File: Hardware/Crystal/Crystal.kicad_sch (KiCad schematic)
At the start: 46 parts, among them J1 USB_B_Micro, U1 AP63205WU, U2 NCP1117-3.3_SOT223, U3 ESP32-C3-WROOM-02, U4 TXS0102DCT, U5 TXS0108EPW

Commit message: Revised L1 for possible 2A output, cleaner fill zones
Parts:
- L1: footprint Inductor_SMD:L_1008_2520Metric_Pad1.43x2.20mm_HandSolder -> Inductor_SMD_Wurth:L_Wurth_WE-LQSH-4020; MFG Murata Electronics -> Wuerth Electronik; PN LQM2HPN4R7MGCL -> 74405042047
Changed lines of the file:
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@@
       (effects (font (size 1.27 1.27)))
     )
-    (property "Footprint" "Inductor_SMD:L_1008_2520Metric_Pad1.43x2.20mm_HandSolder" (at 208.28 30.48 0)
+    (property "Footprint" "Inductor_SMD_Wurth:L_Wurth_WE-LQSH-4020" (at 208.28 30.48 0)
       (effects (font (size 1.27 1.27)) hide)
     )
-    (property "Datasheet" "https://www.mouser.com/datasheet/2/281/1/JELF243B_0025-1634213.pdf" (at 208.28 30.48 0)
+    (property "Datasheet" "https://www.we-online.com/catalog/datasheet/74405042047.pdf" (at 208.28 30.48 0)
       (effects (font (size 1.27 1.27)) hide)
     )
-    (property "MFG" "Murata Electronics" (at 208.28 30.48 0)
+    (property "MFG" "Wuerth Electronik" (at 208.28 30.48 0)
       (effects (font (size 1.27 1.27)) hide)
     )
-    (property "PN" "LQM2HPN4R7MGCL " (at 208.28 30.48 0)
+    (property "PN" "74405042047" (at 208.28 30.48 0)
       (effects (font (size 1.27 1.27)) hide)
     )

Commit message: Added note about VIN plug, BOM cleanup.
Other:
- note added: "Wuerth WR-TBL Plug: Mouser 691361300002 Socket: 691322310002"
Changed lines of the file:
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@@
+    (effects (font (size 1.27 1.27)) (justify left bottom))
+  )
+  (text "Wuerth WR-TBL\nPlug: Mouser 691361300002 \nSocket: 691322310002 "
+    (at 134.62 41.275 0)
     (effects (font (size 1.27 1.27)) (justify left bottom))
   )

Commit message: Checkpoint
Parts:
- added D9: Blue, LED_SMD:LED_1206_3216Metric, symbol Device:LED_Small
- added R17: 1k, Resistor_SMD:R_1206_3216Metric, symbol Device:R
- CB1: now not fitted; now left out of the parts list
- D1: value LED -> Red
- L1: footprint Inductor_SMD_Wurth:L_Wurth_WE-LQSH-4020 -> Inductor_SMD:L_1008_2520Metric_Pad1.43x2.20mm_HandSolder; MFG Wuerth Electronik -> Murata Electronics; PN 74405042047 -> LQM2HPN4R7MGCL
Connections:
- net GND: now also R17.2
- net at TTY1.2 (Pin_2), U4.8 (B1): now also D9.2 (A)
- removed net GPIO18: J1.3 (D+), U3.13 (GPIO18/USB_D-), U5.8 (A7)
- removed net GPIO19: J1.2 (D-), U3.14 (GPIO19/USB_D+), U5.9 (A8)
- new net: D9.1 (K), R17.1
- new net USB_D+: J1.3 (D+), U3.14 (GPIO19/USB_D+)
- new net USB_D-: J1.2 (D-), U3.13 (GPIO18/USB_D-)
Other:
- note removed: "Wuerth WR-TBL Plug: Mouser 691361300002 Socket: 691322310002"
- moved on the sheet: C8, GPIO1, R5, R6, TTY1, U5

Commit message: Final cleanup, added tags for JLCPCB Fabrication
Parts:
- CB1: footprint Capacitor_SMD:CP_Elec_6.3x7.7 -> Capacitor_THT:CP_Radial_D6.3mm_P2.50mm; PN 865080545012 -> 860020573008
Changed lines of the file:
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@@
       (effects (font (size 1.27 1.27)) (justify left))
     )
-    (property "Footprint" "Capacitor_SMD:CP_Elec_6.3x7.7" (at 260.35 25.4 0)
+    (property "Footprint" "Capacitor_THT:CP_Radial_D6.3mm_P2.50mm" (at 260.35 25.4 0)
       (effects (font (size 1.27 1.27)) hide)
     )
@@
       (effects (font (size 1.27 1.27)) hide)
     )
-    (property "PN" "865080545012" (at 260.35 25.4 0)
+    (property "PN" "860020573008" (at 260.35 25.4 0)
       (effects (font (size 1.27 1.27)) hide)
     )

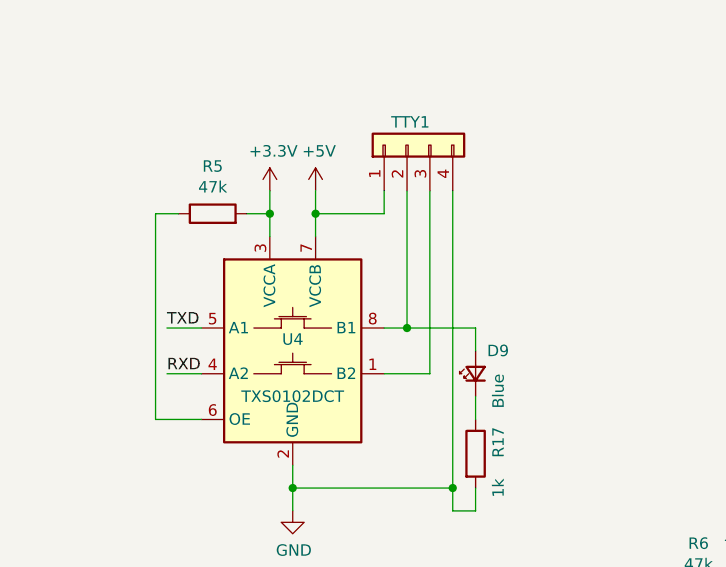
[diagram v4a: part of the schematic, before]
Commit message: Swap TX and RX pins on COM port, populate PCBA data in KiCad
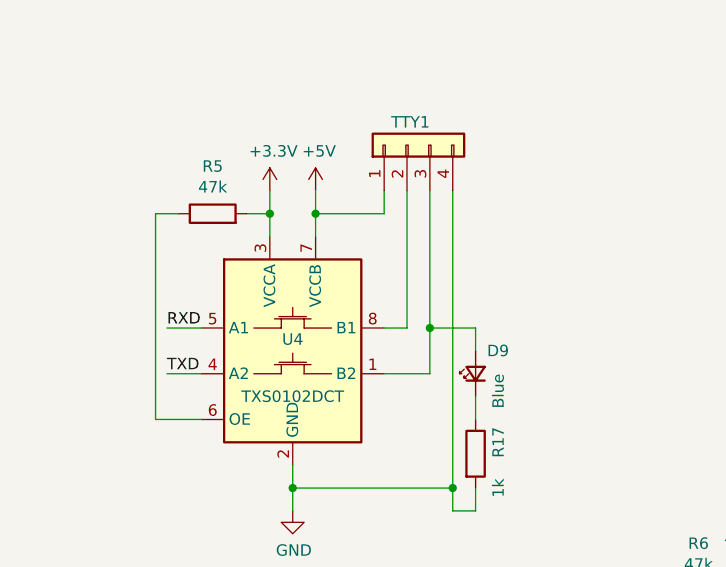
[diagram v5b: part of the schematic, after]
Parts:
- U2: JLCPCB PN (none) -> C91728
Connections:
- net RXD: now also U4.5 (A1); no longer U4.4 (A2)
- net TXD: now also U4.4 (A2); no longer U4.5 (A1)
- net at TTY1.3 (Pin_3), U4.1 (B2): now also D9.2 (A)
- net at TTY1.2 (Pin_2), U4.8 (B1): no longer D9.2 (A)

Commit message: Further board cleanup
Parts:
- removed GPIO1: Conn_01x08_Female, Connector_PinSocket_2.54mm:PinSocket_1x08_P2.54mm_Vertical, symbol ESP32-C3 WIFI-rescue:Conn_01x08_Female-Connector
- added GPIO1: Conn_01x06, Connector_PinSocket_2.54mm:PinSocket_1x06_P2.54mm_Vertical, symbol Connector_Generic:Conn_01x06
- BOOT1, RESET1: footprint Button_Switch_SMD:SW_SPST_B3U-3000P -> Button_Switch_SMD:SW_SPST_B3U-3000P-B
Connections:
- net at U5.14 (B6): now also GPIO1.6 (Pin_6)
- net at U5.15 (B5): now also GPIO1.5 (Pin_5)
- net at U5.16 (B4): now also GPIO1.4 (Pin_4)
- net at U5.17 (B3): now also GPIO1.3 (Pin_3)
- net at U5.18 (B2): now also GPIO1.2 (Pin_2)
- net at U5.20 (B1): now also GPIO1.1 (Pin_1)
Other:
- moved on the sheet: C8, R6, U5

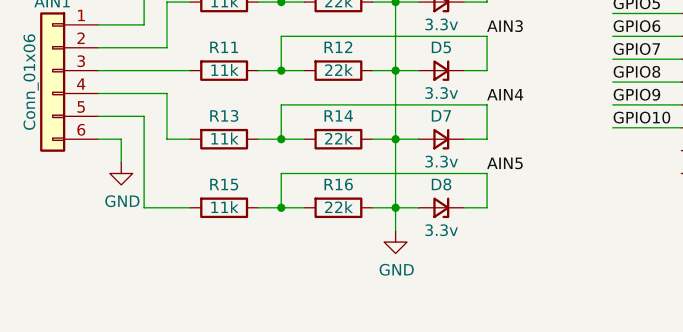
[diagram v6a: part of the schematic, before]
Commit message: Changed mounting holes to be drilled and plated instead of milled.
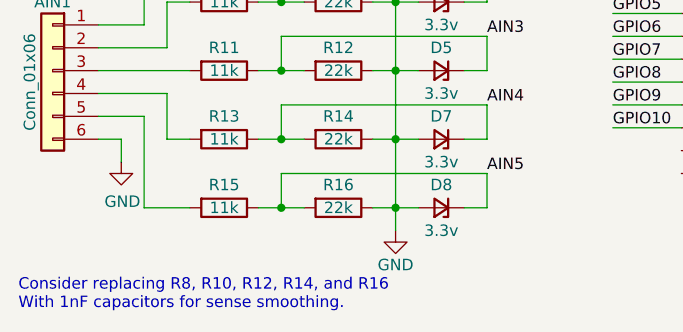
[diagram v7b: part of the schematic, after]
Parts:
- U2: JLCPCB PN C91728 -> (none)
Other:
- note added: "Consider replacing R8, R10, R12, R14, and R16 With 1nF capacitors for sense smoothing."
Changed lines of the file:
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@@
   (title_block
     (title "Crystal - ESP32-C3 wifi adapter")
-    (date "2023-07-26")
+    (date "2023-12-30")
+    (rev "0.4")
     (company "SeraphimLabs LLC")
   )
@@
     (effects (font (size 1.27 1.27)) (justify left bottom))
   )
+  (text "Consider replacing R8, R10, R12, R14, and R16\nWith 1nF capacitors for sense smoothing. "
+    (at 12.7 203.2 0)
+    (effects (font (size 1.27 1.27)) (justify left bottom))
+  )
   (text "Use ESP32-C3-WROOM-02-N4 " (at 160.02 175.26 0)
     (effects (font (size 1.27 1.27)) (justify left bottom))
@@
       (effects (font (size 1.27 1.27)) hide)
     )
-    (property "JLCPCB PN" "" (at 96.52 177.8 0)
-      (effects (font (size 1.27 1.27)) hide)
-    )
     (pin "1")
     (pin "10")
@@
       (effects (font (size 1.27 1.27)) hide)
     )
-    (property "JLCPCB PN" "" (at 34.29 22.86 0)
-      (effects (font (size 1.27 1.27)) hide)
-    )
     (pin "1")
     (pin "2")
@@
       (effects (font (size 1.27 1.27)) hide)
     )
-    (property "JLCPCB PN" "" (at 43.18 129.54 0)
-      (effects (font (size 1.27 1.27)) hide)
-    )
     (pin "1")
     (pin "2")
@@
       (effects (font (size 1.27 1.27)) hide)
     )
-    (property "JLCPCB PN" "" (at 48.26 191.77 0)
-      (effects (font (size 1.27 1.27)) hide)
-    )
     (pin "1")
     (pin "2")
@@
       (effects (font (size 1.27 1.27)) hide)
     )
-    (property "JLCPCB PN" "" (at 35.56 191.77 0)
-      (effects (font (size 1.27 1.27)) hide)
-    )
     (pin "1")
     (pin "2")
@@
       (effects (font (size 1.27 1.27)) hide)
     )
-    (property "JLCPCB PN" "" (at 59.69 191.77 0)
-      (effects (font (size 1.27 1.27)) hide)
-    )
     (pin "1")
     (pin "2")
@@
       (effects (font (size 1.27 1.27)) hide)
     )
-    (property "Value" "GND" (at 54.737 198.7042 0)
+    (property "Value" "GND" (at 54.61 198.12 0)
       (effects (font (size 1.27 1.27)))
     )
@@
       (effects (font (size 1.27 1.27)) hide)
     )
-    (property "JLCPCB PN" "" (at 48.26 184.15 0)
-      (effects (font (size 1.27 1.27)) hide)
-    )
     (pin "1")
     (pin "2")
@@
       (effects (font (size 1.27 1.27)) hide)
     )
-    (property "JLCPCB PN" "" (at 35.56 184.15 0)
-      (effects (font (size 1.27 1.27)) hide)
-    )
     (pin "1")
     (pin "2")
@@
       (effects (font (size 1.27 1.27)) hide)
     )
-    (property "JLCPCB PN" "" (at 59.69 184.15 0)
-      (effects (font (size 1.27 1.27)) hide)
-    )
     (pin "1")
     (pin "2")
@@
       (effects (font (size 1.27 1.27)) hide)
     )
-    (property "JLCPCB PN" "" (at 48.26 176.53 0)
-      (effects (font (size 1.27 1.27)) hide)
-    )
     (pin "1")
     (pin "2")
@@
       (effects (font (size 1.27 1.27)) hide)
     )
-    (property "JLCPCB PN" "" (at 35.56 176.53 0)
-      (effects (font (size 1.27 1.27)) hide)
-    )
     (pin "1")
     (pin "2")
@@
       (effects (font (size 1.27 1.27)) hide)
     )
-    (property "JLCPCB PN" "" (at 59.69 176.53 0)
-      (effects (font (size 1.27 1.27)) hide)
-    )
     (pin "1")
     (pin "2")
@@
       (effects (font (size 1.27 1.27)) hide)
     )
-    (property "JLCPCB PN" "" (at 48.26 168.91 0)
-      (effects (font (size 1.27 1.27)) hide)
-    )
     (pin "1")
     (pin "2")
@@
       (effects (font (size 1.27 1.27)) hide)
     )
-    (property "JLCPCB PN" "" (at 35.56 168.91 0)
-      (effects (font (size 1.27 1.27)) hide)
-    )
     (pin "1")
     (pin "2")
@@
       (effects (font (size 1.27 1.27)) hide)
     )
-    (property "JLCPCB PN" "" (at 59.69 168.91 0)
-      (effects (font (size 1.27 1.27)) hide)
-    )
     (pin "1")
     (pin "2")
@@
       (effects (font (size 1.27 1.27)) hide)
     )
-    (property "JLCPCB PN" "" (at 48.26 161.29 0)
-      (effects (font (size 1.27 1.27)) hide)
-    )
     (pin "1")
     (pin "2")
@@
       (effects (font (size 1.27 1.27)) hide)
     )
-    (property "JLCPCB PN" "" (at 35.56 161.29 0)
-      (effects (font (size 1.27 1.27)) hide)
-    )
     (pin "1")
     (pin "2")
@@
       (effects (font (size 1.27 1.27)) hide)
     )
-    (property "JLCPCB PN" "" (at 59.69 161.29 0)
-      (effects (font (size 1.27 1.27)) hide)
-    )
     (pin "1")
     (pin "2")
@@
       (effects (font (size 1.27 1.27)) hide)
     )
-    (property "JLCPCB PN" "" (at 22.86 27.94 0)
-      (effects (font (size 1.27 1.27)) hide)
-    )
     (pin "1")
     (pin "2")
@@
       (effects (font (size 1.27 1.27)) hide)
     )
-    (property "JLCPCB PN" "" (at 55.88 106.68 0)
-      (effects (font (size 1.27 1.27)) hide)
-    )
     (pin "1")
     (pin "2")
@@
       (effects (font (size 1.27 1.27)) hide)
     )
-    (property "JLCPCB PN" "" (at 16.51 176.53 0)
-      (effects (font (size 1.27 1.27)) hide)
-    )
     (pin "1")
     (pin "2")
@@
       (effects (font (size 1.27 1.27)) hide)
     )
-    (property "JLCPCB PN" "" (at 34.29 114.3 0)
-      (effects (font (size 1.27 1.27)) hide)
-    )
     (pin "1")
     (pin "2")
@@
       (effects (font (size 1.27 1.27)) hide)
     )
-    (property "JLCPCB PN" "C91728" (at 228.6 35.56 0)
-      (effects (font (size 1.27 1.27)) hide)
-    )
     (pin "1")
     (pin "2")
@@
       (effects (font (size 1.27 1.27)) hide)
     )
-    (property "JLCPCB PN" "" (at 179.07 33.02 0)
-      (effects (font (size 1.27 1.27)) hide)
-    )
     (pin "1")
     (pin "2")
@@
       (effects (font (size 1.27 1.27)) hide)
     )
-    (property "JLCPCB PN" "" (at 166.37 40.64 0)
-      (effects (font (size 1.27 1.27)) hide)
-    )
     (pin "1")
     (pin "2")
@@
       (effects (font (size 1.27 1.27)) hide)
     )
-    (property "JLCPCB PN" "" (at 208.28 30.48 0)
-      (effects (font (size 1.27 1.27)) hide)
-    )
     (pin "1")
     (pin "2")
@@
       (effects (font (size 1.27 1.27)) hide)
     )
-    (property "JLCPCB PN" "" (at 199.39 38.1 0)
-      (effects (font (size 1.27 1.27)) hide)
-    )
     (pin "1")
     (pin "2")
@@
       (effects (font (size 1.27 1.27)) hide)
     )
-    (property "JLCPCB PN" "" (at 63.5 140.97 0)
-      (effects (font (size 1.27 1.27)) hide)
-    )
     (pin "1")
     (pin "2")
@@
       (effects (font (size 1.27 1.27)) hide)
     )
-    (property "JLCPCB PN" "" (at 208.28 40.64 0)
-      (effects (font (size 1.27 1.27)) hide)
-    )
     (pin "1")
     (pin "2")
@@
       (effects (font (size 1.27 1.27)) hide)
     )
-    (property "JLCPCB PN" "" (at 88.9 156.21 0)
-      (effects (font (size 1.27 1.27)) hide)
-    )
     (pin "1")
     (pin "2")
@@
       (effects (font (size 1.27 1.27)) hide)
     )
-    (property "JLCPCB PN" "" (at 82.55 22.86 0)
-      (effects (font (size 1.27 1.27)) hide)
-    )
     (pin "1")
     (pin "2")
@@
       (effects (font (size 1.27 1.27)) hide)
     )
-    (property "JLCPCB PN" "" (at 217.17 40.64 0)
-      (effects (font (size 1.27 1.27)) hide)
-    )
     (pin "1")
     (pin "2")
@@
       (effects (font (size 1.27 1.27)) hide)
     )
-    (property "JLCPCB PN" "" (at 260.35 25.4 0)
-      (effects (font (size 1.27 1.27)) hide)
-    )
     (pin "1")
     (pin "2")
@@
       (effects (font (size 1.27 1.27)) hide)
     )
-    (property "JLCPCB PN" "" (at 116.84 175.26 0)
-      (effects (font (size 1.27 1.27)) hide)
-    )
     (pin "1")
     (pin "2")
@@
       (effects (font (size 1.27 1.27)) hide)
     )
-    (property "JLCPCB PN" "" (at 238.76 40.64 0)
-      (effects (font (size 1.27 1.27)) hide)
-    )
     (pin "1")
     (pin "2")
@@
       (effects (font (size 1.27 1.27)) hide)
     )
-    (property "JLCPCB PN" "" (at 255.27 26.67 0)
-      (effects (font (size 1.27 1.27)) hide)
-    )
     (pin "1")
     (pin "2")
@@
       (effects (font (size 1.27 1.27)) hide)
     )
-    (property "JLCPCB PN" "" (at 58.42 50.8 0)
-      (effects (font (size 1.27 1.27)) hide)
-    )
     (pin "1")
     (pin "10")
@@
       (effects (font (size 1.27 1.27)) hide)
     )
-    (property "JLCPCB PN" "" (at 19.05 30.48 0)
-      (effects (font (size 1.27 1.27)) hide)
-    )
     (pin "1")
     (pin "2")
@@
       (effects (font (size 1.27 1.27)) hide)
     )
-    (property "JLCPCB PN" "" (at 96.52 27.94 0)
-      (effects (font (size 1.27 1.27)) hide)
-    )
     (pin "1")
     (pin "2")
@@
       (effects (font (size 1.27 1.27)) hide)
     )
-    (property "JLCPCB PN" "" (at 148.59 177.8 0)
-      (effects (font (size 1.27 1.27)) hide)
-    )
     (pin "1")
     (pin "2")
@@
       (effects (font (size 1.27 1.27)) hide)
     )
-    (property "JLCPCB PN" "" (at 68.58 20.32 0)
-      (effects (font (size 1.27 1.27)) hide)
-    )
     (pin "1")
     (pin "2")
@@
       (effects (font (size 1.27 1.27)) hide)
     )
-    (property "JLCPCB PN" "" (at 100.33 30.48 0)
-      (effects (font (size 1.27 1.27)) hide)
-    )
     (pin "1")
     (pin "2")
@@
       (effects (font (size 1.27 1.27)) hide)
     )
-    (property "JLCPCB PN" "" (at 80.01 156.21 0)
-      (effects (font (size 1.27 1.27)) hide)
-    )
     (pin "1")
     (pin "2")
@@
       (effects (font (size 1.27 1.27)) hide)
     )
-    (property "JLCPCB PN" "" (at 63.5 132.08 0)
-      (effects (font (size 1.27 1.27)) hide)
-    )
     (pin "1")
     (pin "2")
@@
       (effects (font (size 1.27 1.27)) hide)
     )
-    (property "JLCPCB PN" "" (at 138.43 182.88 0)
-      (effects (font (size 1.27 1.27)) hide)
-    )
     (pin "1")
     (pin "2")
@@
       (effects (font (size 1.27 1.27)) hide)
     )
-    (property "JLCPCB PN" "" (at 156.21 30.48 0)
-      (effects (font (size 1.27 1.27)) hide)
-    )
     (pin "1")
     (pin "2")
@@
       (effects (font (size 1.27 1.27)) hide)
     )
-    (property "JLCPCB PN" "" (at 193.04 41.91 0)
-      (effects (font (size 1.27 1.27)) hide)
-    )
     (pin "1")
     (pin "2")
@@
       (effects (font (size 1.27 1.27)) hide)
     )
-    (property "JLCPCB PN" "" (at 194.31 33.02 0)
-      (effects (font (size 1.27 1.27)) hide)
-    )
